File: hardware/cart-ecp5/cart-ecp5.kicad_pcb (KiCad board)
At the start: 4 copper layers, 100 x 60 mm, 129 parts, among them J1 JTAG, J2 MicroSD_Molex_1040310811, J3 N64_Cartridge_Bus, J5 USB_C_USB2.0, U1 LFE5U-25F-xBG256x, U10 93C46BT-I_OT, U11 FT2232HQ, U13 TLV62568DBV, U2 W25Q512JVEIM, U3 S27KS0641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

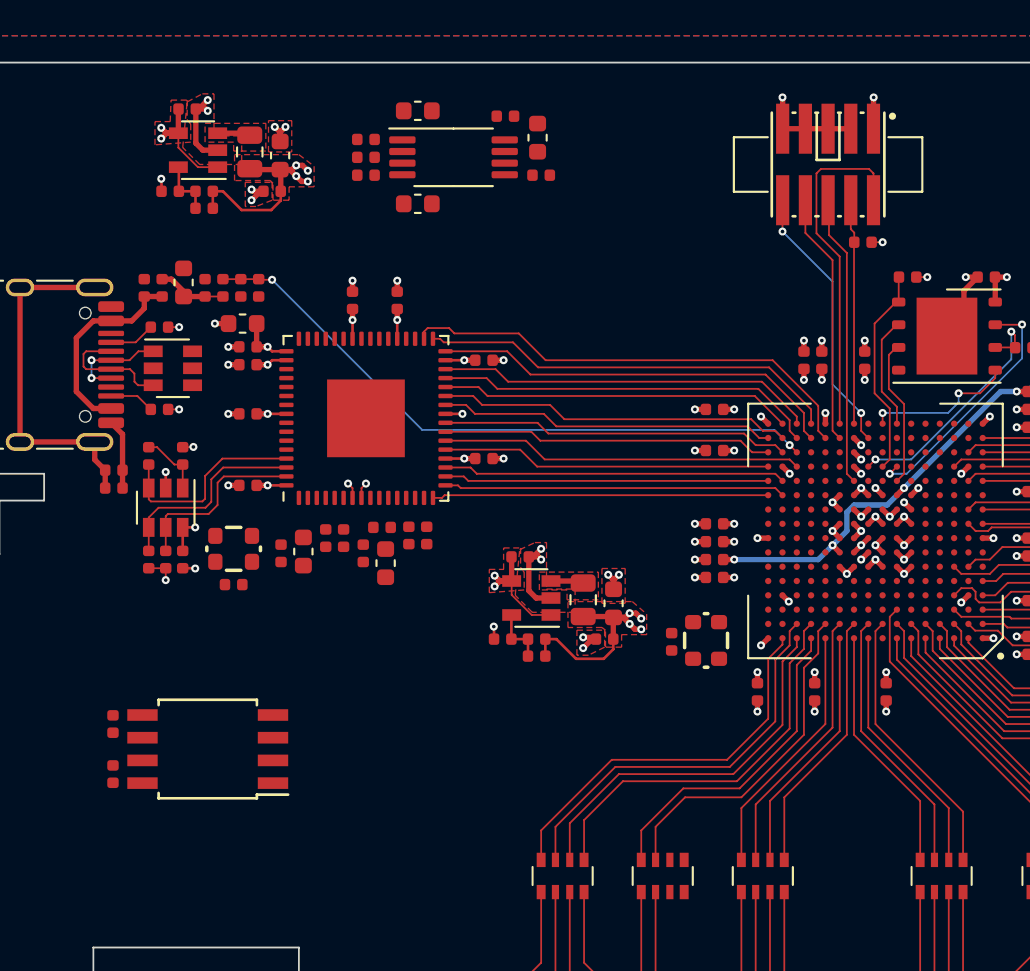
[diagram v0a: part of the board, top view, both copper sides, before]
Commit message: Route power mux with traces
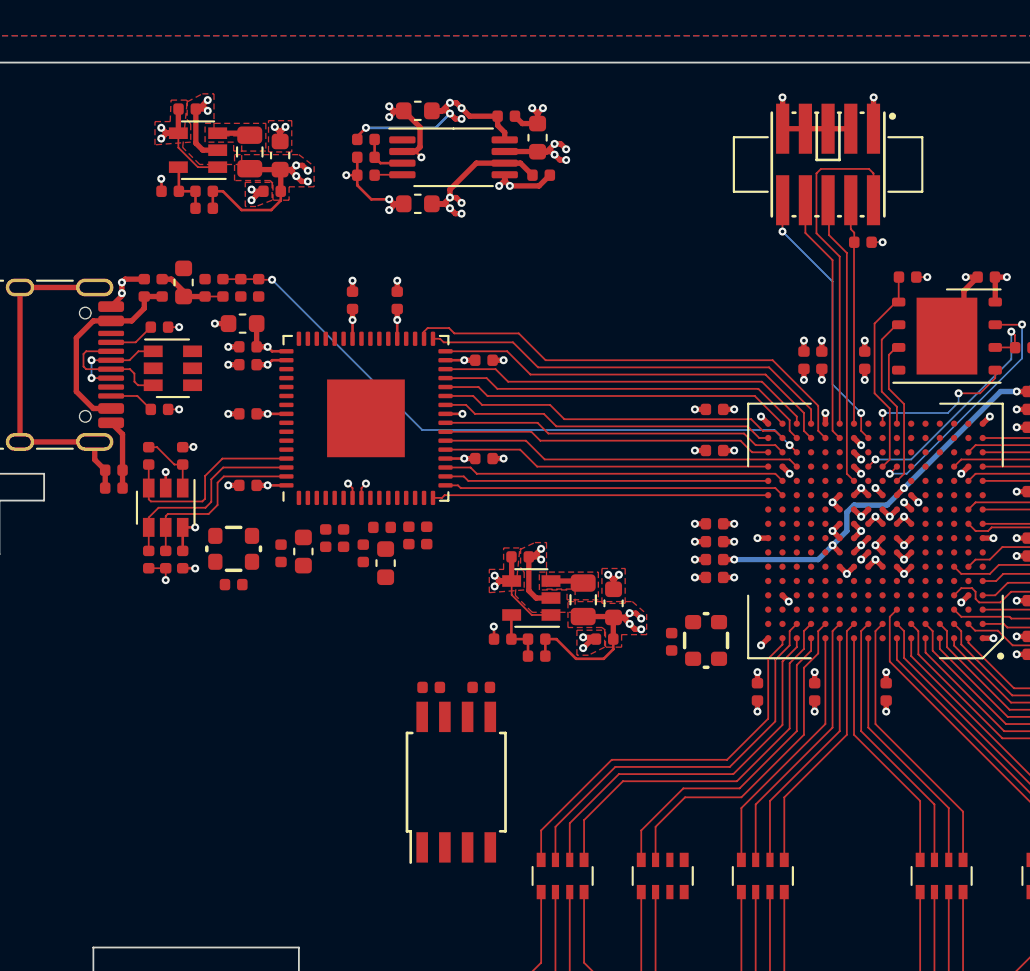
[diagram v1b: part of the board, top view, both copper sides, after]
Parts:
- moved R6 20.7 mm to (128.0, 109.0), turned to 0 degrees
- moved C41 18.4 mm to (125.2, 109.0), turned to 0 degrees
- moved U4 14.0 mm to (126.5, 114.2), turned to 90 degrees
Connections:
- R7 pad 1: USB_3V3 -> N64_3V3
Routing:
- net GND: track 98.4 -> 178.9 mm, vias 93 -> 105
- net N64_3V3: track 0.00 -> 13.4 mm, vias 0 -> 5
- net USB_3V3: track 12.5 -> 22.2 mm, vias 4 -> 8
- net P3V3: track 56.1 -> 61.6 mm, vias 37 -> 41
- net Net-(R7-Pad2): track 0.00 -> 2.69 mm
- net Net-(R9-Pad1): track 0.00 -> 1.56 mm

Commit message: Add copper zones for power mux
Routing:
- net N64_3V3: track 13.4 -> 14.5 mm
- net GND: track 178.9 -> 179.7 mm
- added copper zone on F.Cu, net N64_3V3

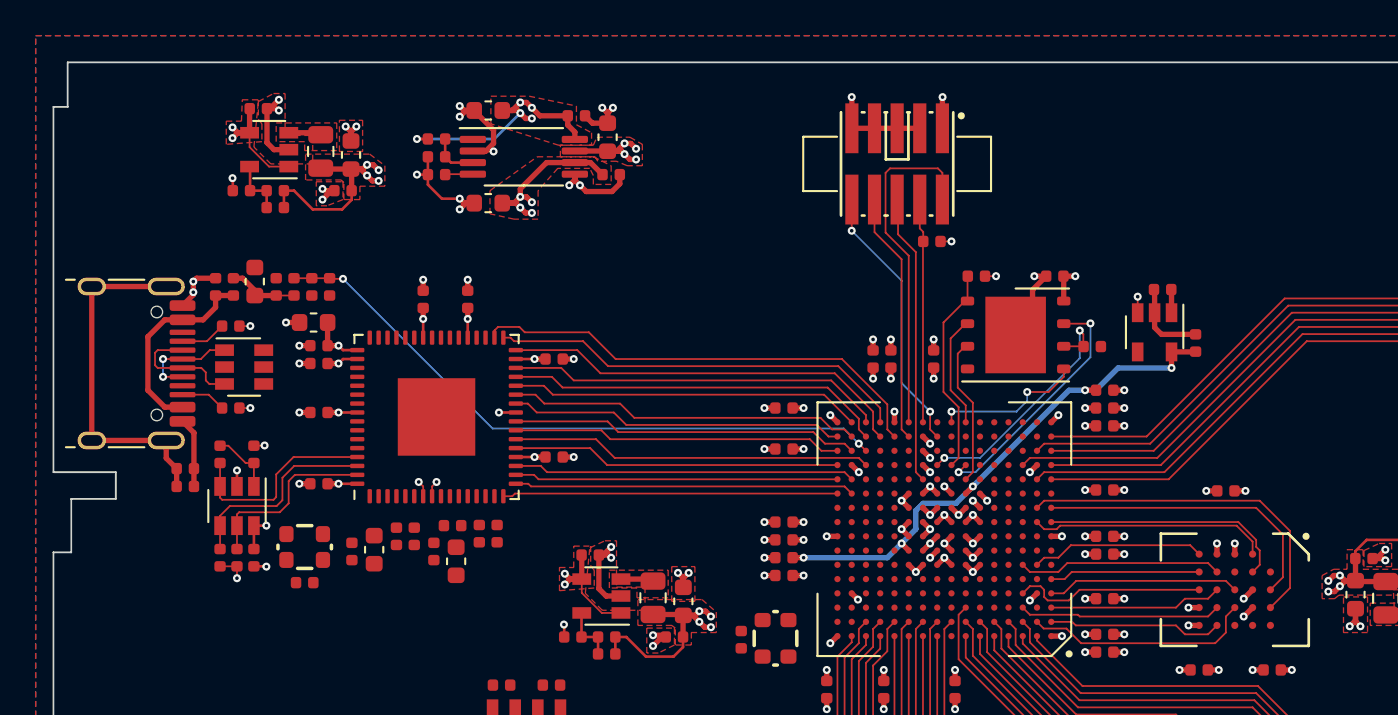
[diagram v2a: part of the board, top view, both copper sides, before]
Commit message: Move JTAG connector to make space for logo
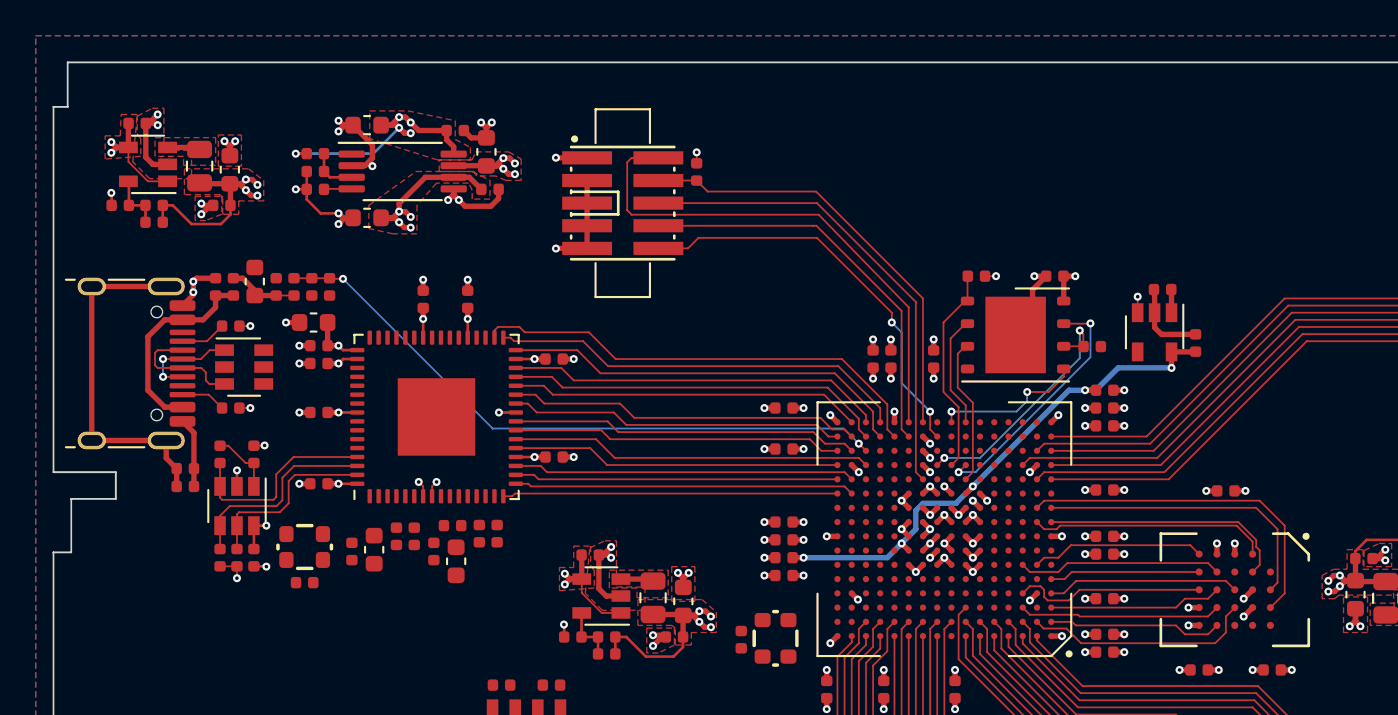
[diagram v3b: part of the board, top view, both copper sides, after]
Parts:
- moved J1 15.6 mm to (131.9, 81.9), turned to 90 degrees
- moved R3 13.8 mm to (136.1, 80.2), turned to 270 degrees
- moved C5 6.85 mm to (117.6, 77.5)
- moved C8 6.85 mm to (124.5, 81.1)
- moved U5 6.85 mm to (119.6, 80.1)
- moved C7 6.85 mm to (117.6, 82.7)
- moved C10 6.85 mm to (104.7, 77.4)
- moved C16 6.85 mm to (109.9, 80.0)
- moved C18 6.85 mm to (109.5, 82.0)
- moved C6 6.85 mm to (122.5, 77.8)
- moved C9 6.85 mm to (124.3, 79.0)
- moved L1 6.85 mm to (108.2, 79.8)
- moved R10 6.85 mm to (105.7, 82.0)
- moved R11 6.85 mm to (103.8, 82.0)
- moved R7 6.85 mm to (114.7, 79.1)
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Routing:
- net /FPGA-IO/JTAG_TCK: track 12.7 -> 24.5 mm
- net /FPGA-IO/JTAG_TDO: track 16.3 -> 26.9 mm
- net /FPGA-IO/JTAG_TMS: track 19.4 -> 29.1 mm
- net /FPGA-IO/JTAG_TDI: track 14.1 -> 22.8 mm
- net /FPGA-IO/FPGA_RESET: track 15.3 -> 23.1 mm

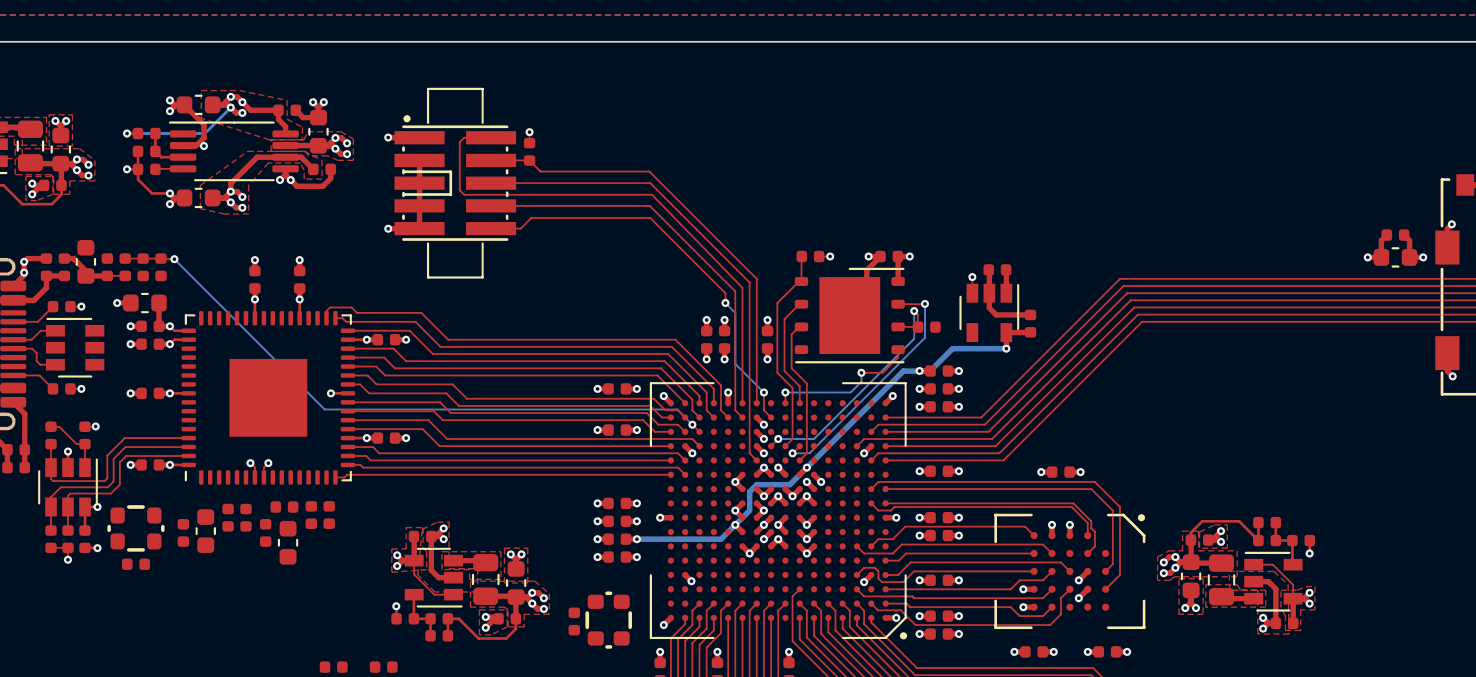
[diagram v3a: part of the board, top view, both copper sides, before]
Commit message: Add temporary logo to PCB
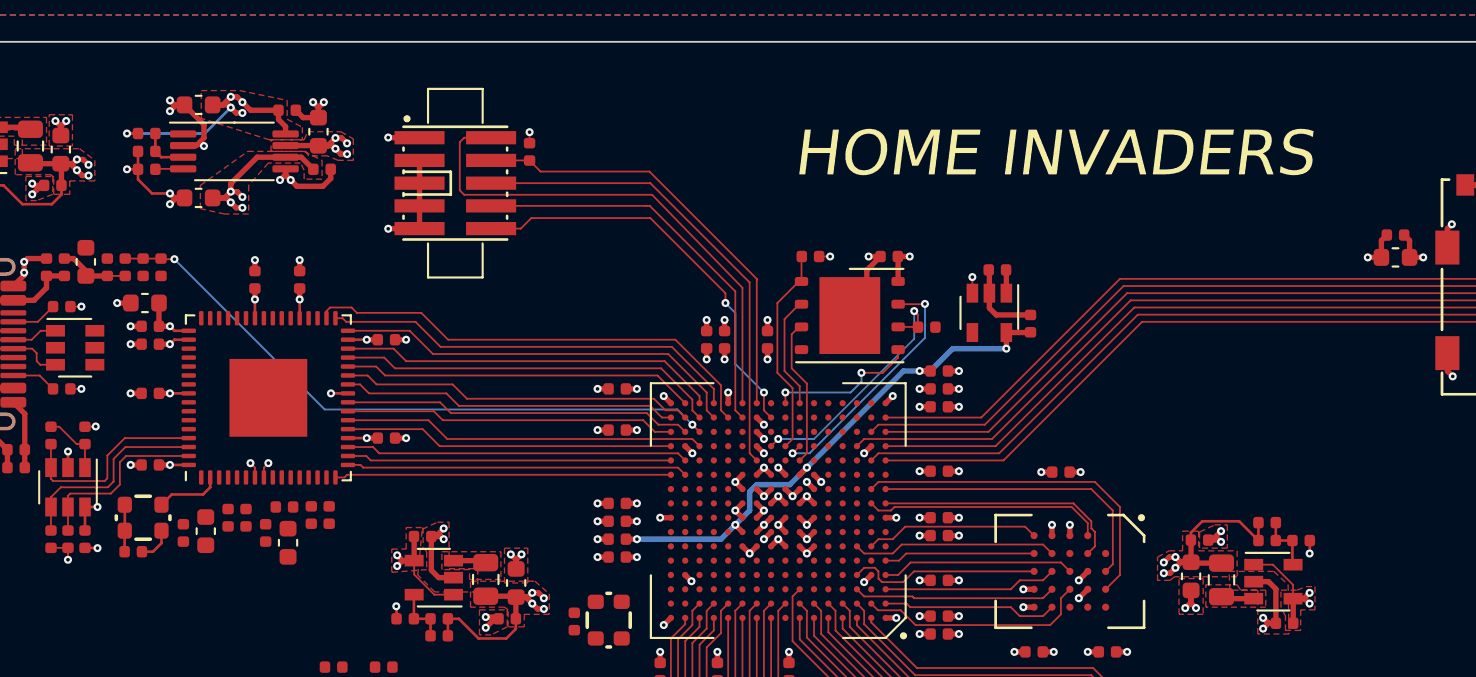
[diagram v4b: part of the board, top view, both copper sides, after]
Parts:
- moved X2 0.72 mm to (114.5, 100.6)
- moved C37 0.72 mm to (114.0, 102.5)
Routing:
- net /Interface-USB/USB_CLK: track 0.00 -> 3.68 mm
- net P3V3: track 61.6 -> 64.2 mm
- net GND: track 179.7 -> 181.7 mm
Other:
- board text added: "HOME INVADERS"
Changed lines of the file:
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@@
   (general
     (thickness 1.2)
-    (drawings 35)
-    (tracks 1307)
+    (drawings 36)
+    (tracks 1317)
     (zones 0)
     (modules 129)
@@
   )
   (setup
-    (last_trace_width 0.1)
+    (last_trace_width 0.15)
     (user_trace_width 0.1)
     (user_trace_width 0.15)
@@
   )
   (module Capacitor_SMD:C_0402_1005Metric (layer F.Cu)
-    (at 114.1 103.2)
+    (at 113.95 102.5)
     (descr "Capacitor SMD 0402 (1005 Metric), square (rectangular) end terminal, IPC_7351 nominal, (Body size source: http://www.tortai-tech.com/upload/download/2011102023233369053.pdf), generated with kicad-footprint-generator")
     (tags capacitor)
@@
   )
   (module ng_time:Oscillator_2.5x2.0 (layer F.Cu)
-    (at 114.1 101.2)
+    (at 114.5 100.6)
     (fp_text reference X2 (at 0.7 -2.1) (layer F.SilkS) hide
       (effects (font (size 1 1) (thickness 0.15)))
@@
       (net 1 GND) (zone_connect 2))
   )
+  (gr_text "HOME INVADERS" (at 165.4 80.25) (layer F.SilkS)
+    (effects (font (size 2.5 2.5) (thickness 0.3) italic))
+  )
   (gr_line (start 112.8 121.9) (end 112.8 134.5) (layer Dwgs.User) (width 0.15))
   (gr_line (start 187.2 121.9) (end 187.2 134.5) (layer Dwgs.User) (width 0.15))
@@
   (segment (start 116.000024 77.875) (end 117.9 79.774976) (width 0.3) (layer "In1.Cu(GND)") (net 1))
   (segment (start 120.250006 79.825) (end 117.9 79.825) (width 0.3) (layer "In1.Cu(GND)") (net 1))
+  (segment (start 114.435 102.5) (end 115.05 102.5) (width 0.15) (layer F.Cu) (net 1))
+  (segment (start 115.524999 102.025001) (end 115.524999 101.325) (width 0.15) (layer F.Cu) (net 1))
+  (segment (start 115.05 102.5) (end 115.524999 102.025001) (width 0.15) (layer F.Cu) (net 1))
   (via (at 128.7 103.299994) (size 0.45) (drill 0.2) (layers F.Cu B.Cu) (net 2))
   (via (at 128.699976 102.7) (size 0.45) (drill 0.2) (layers F.Cu B.Cu) (net 2))
@@
   (segment (start 124.2875 79.8) (end 124.3 79.8125) (width 0.3) (layer F.Cu) (net 2))
   (segment (start 122.4625 79.8) (end 124.2875 79.8) (width 0.3) (layer F.Cu) (net 2))
+  (segment (start 113.475 99.875) (end 113.475 101.325) (width 0.15) (layer F.Cu) (net 2))
+  (segment (start 113.465 101.335) (end 113.475 101.325) (width 0.15) (layer F.Cu) (net 2))
+  (segment (start 113.465 102.5) (end 113.465 101.335) (width 0.15) (layer F.Cu) (net 2))
   (segment (start 160.3 116) (end 160.3 118.6) (width 0.1) (layer F.Cu) (net 3))
   (segment (start 151.6 107.3) (end 160.3 116) (width 0.1) (layer F.Cu) (net 3))
@@
   (segment (start 125.75 98.35) (end 125.9 98.2) (width 0.1) (layer F.Cu) (net 277))
   (segment (start 125.25 98.35) (end 125.75 98.35) (width 0.1) (layer F.Cu) (net 277))
+  (segment (start 117.85 99.3) (end 116.099999 99.3) (width 0.15) (layer F.Cu) (net 279))
+  (segment (start 118.25 98.9) (end 117.85 99.3) (width 0.15) (layer F.Cu) (net 279))
+  (segment (start 116.099999 99.3) (end 115.524999 99.875) (width 0.15) (layer F.Cu) (net 279))
+  (segment (start 118.25 98.35) (end 118.25 98.9) (width 0.15) (layer F.Cu) (net 279))
   (via (at 130 125.65) (size 0.45) (drill 0.2) (layers F.Cu B.Cu) (net 281))
   (segment (start 130 130) (end 130 125.65) (width 0.1) (layer B.Cu) (net 281))
@@
   (segment (start 133.7 124.35) (end 133.7 120.4) (width 0.1) (layer F.Cu) (net 282))
   (segment (start 135 125.65) (end 133.7 124.35) (width 0.1) (layer F.Cu) (net 282))
-  (segment (start 167.7 98.6) (end 169.1 100) (width 0.1) (layer F.Cu) (net 284))
   (segment (start 169.1 103.8) (end 168.3 104.6) (width 0.1) (layer F.Cu) (net 284))
   (segment (start 169.1 100) (end 169.1 103.8) (width 0.1) (layer F.Cu) (net 284))
+  (segment (start 167.7 98.6) (end 169.1 100) (width 0.1) (layer F.Cu) (net 284))
   (segment (start 155.6 98.6) (end 167.7 98.6) (width 0.1) (layer F.Cu) (net 284))
   (segment (start 155.2 99) (end 155.6 98.6) (width 0.1) (layer F.Cu) (net 284))
